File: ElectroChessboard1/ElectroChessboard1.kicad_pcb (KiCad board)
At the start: 2 copper layers, 306.2 x 314.8 mm, 243 parts, among them IC1 A3213ELHLT-T, IC10 A3213ELHLT-T, IC11 A3213ELHLT-T, IC12 A3213ELHLT-T, IC13 A3213ELHLT-T, IC14 A3213ELHLT-T, IC15 A3213ELHLT-T, IC16 A3213ELHLT-T, IC17 A3213ELHLT-T, IC18 ADG708BRUZ-REEL7, IC19 A3213ELHLT-T, IC2 A3213ELHLT-T, IC20 A3213ELHLT-T, IC21 A3213ELHLT-T, IC22 A3213ELHLT-T, IC23 A3213ELHLT-T, IC24 A3213ELHLT-T, IC25 A3213ELHLT-T, IC26 A3213ELHLT-T, IC27 A3213ELHLT-T, IC28 A3213ELHLT-T, IC29 A3213ELHLT-T, IC3 A3213ELHLT-T, IC30 A3213ELHLT-T, IC31 A3213ELHLT-T, IC32 A3213ELHLT-T, IC33 A3213ELHLT-T, IC34 A3213ELHLT-T, IC35 ADG708BRUZ-REEL7, IC36 ADG708BRUZ-REEL7, IC37 A3213ELHLT-T, IC38 A3213ELHLT-T, IC39 A3213ELHLT-T, IC4 A3213ELHLT-T, IC40 A3213ELHLT-T, IC41 A3213ELHLT-T, IC42 A3213ELHLT-T, IC43 A3213ELHLT-T, IC44 A3213ELHLT-T, IC45 A3213ELHLT-T, IC46 A3213ELHLT-T, IC47 A3213ELHLT-T, IC48 A3213ELHLT-T, IC49 A3213ELHLT-T, IC5 A3213ELHLT-T, IC50 A3213ELHLT-T, IC51 A3213ELHLT-T, IC52 A3213ELHLT-T, IC53 ADG708BRUZ-REEL7, IC54 ADG708BRUZ-REEL7, IC55 A3213ELHLT-T, IC56 A3213ELHLT-T, IC57 A3213ELHLT-T, IC58 A3213ELHLT-T, IC59 A3213ELHLT-T, IC6 A3213ELHLT-T, IC60 A3213ELHLT-T, IC61 A3213ELHLT-T, IC62 A3213ELHLT-T, IC63 A3213ELHLT-T, IC64 A3213ELHLT-T, IC65 A3213ELHLT-T, IC66 A3213ELHLT-T, IC67 A3213ELHLT-T, IC68 A3213ELHLT-T, IC69 A3213ELHLT-T, IC7 A3213ELHLT-T, IC70 A3213ELHLT-T, IC71 ADG708BRUZ-REEL7, IC72 ADG708BRUZ-REEL7, IC73 CD74HC154M96, IC74 CD74HC154M96, IC75 DS1307Z+T&R, IC76 CD74HC154M96, IC77 CD74HC154M96, IC8 A3213ELHLT-T, IC9 ADG708BRUZ-REEL7, J2 TYPE-C-31-M-12, J3 Conn_01x04_Pin, J5 Conn_01x06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

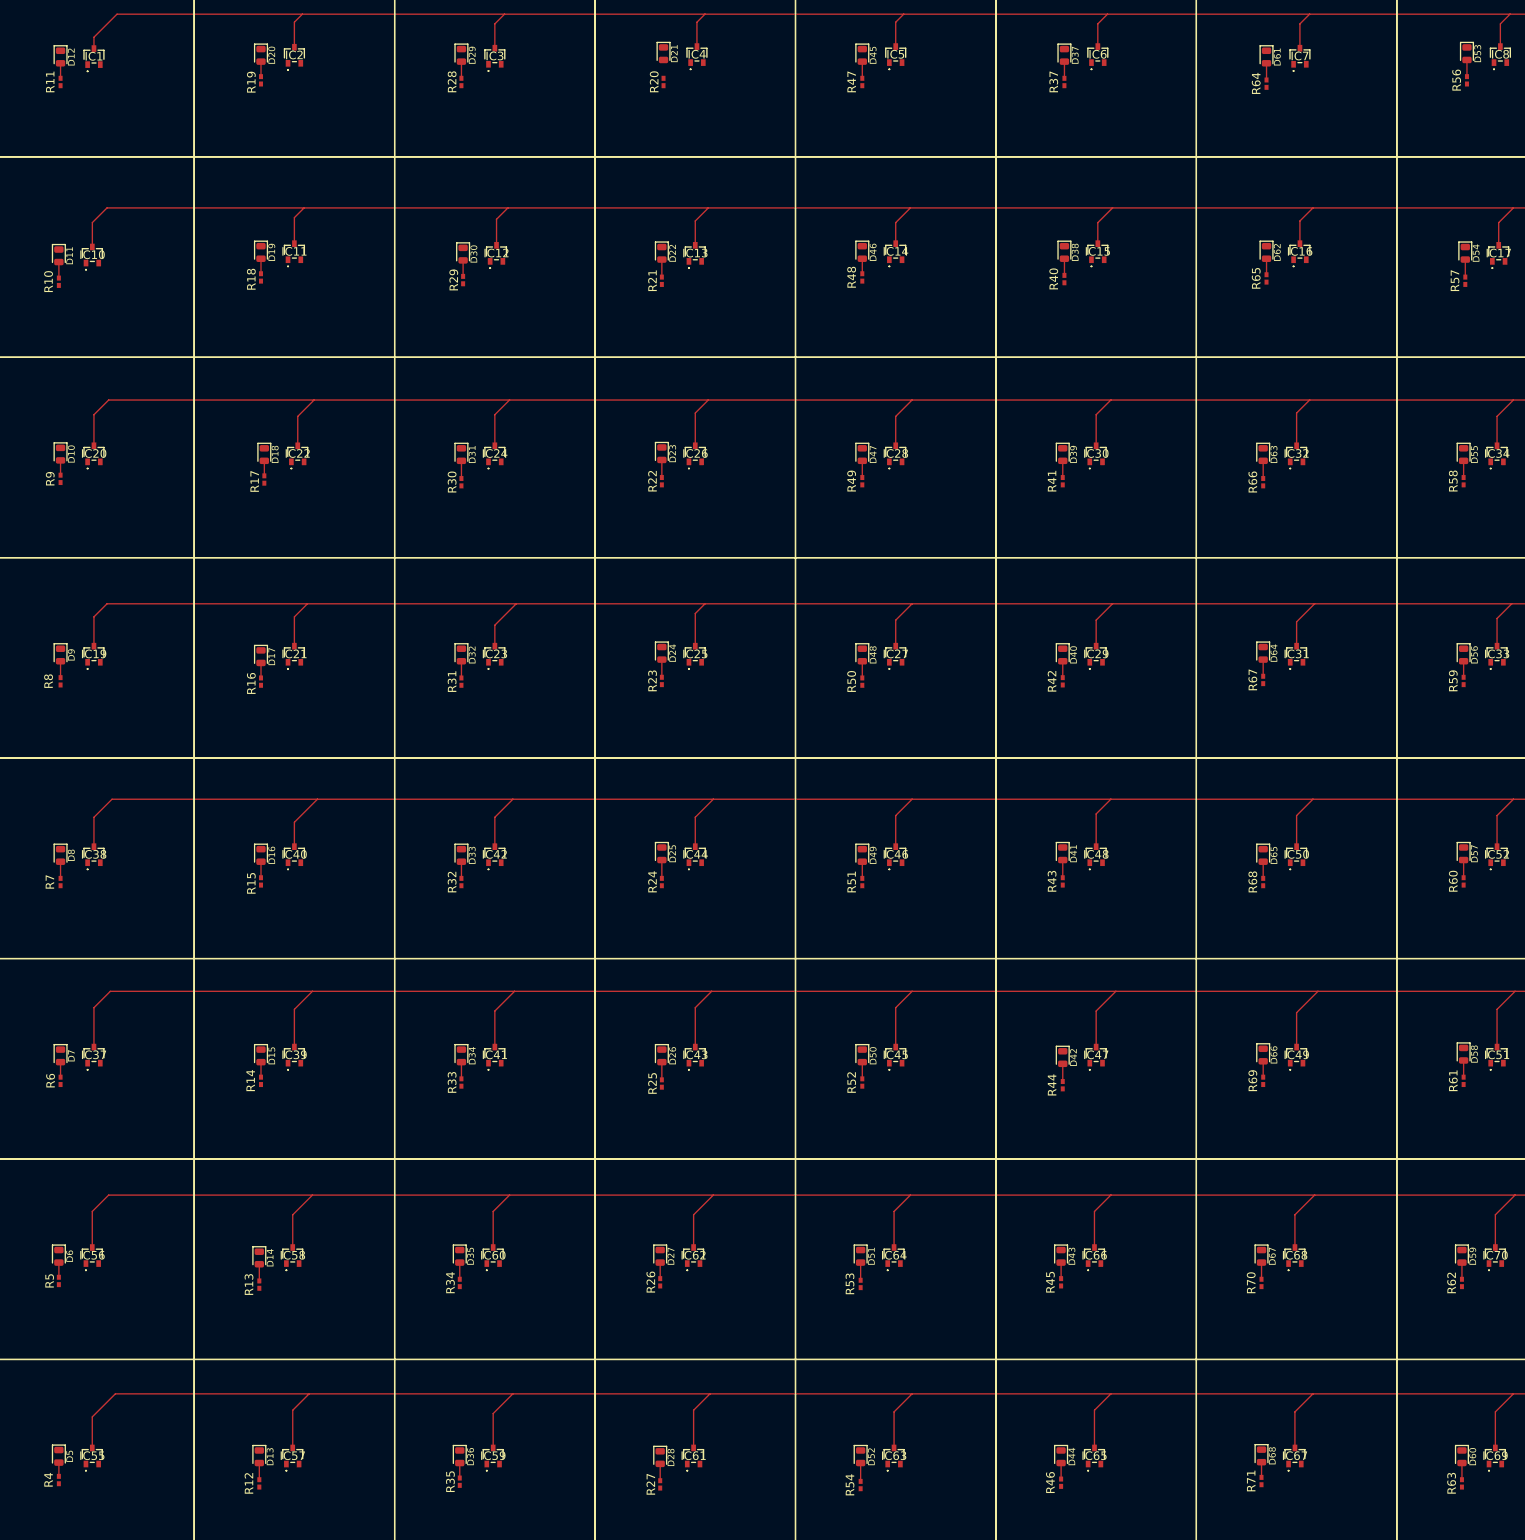
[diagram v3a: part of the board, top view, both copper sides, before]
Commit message: Rotated all LEDs on PCB 180 degrees
.
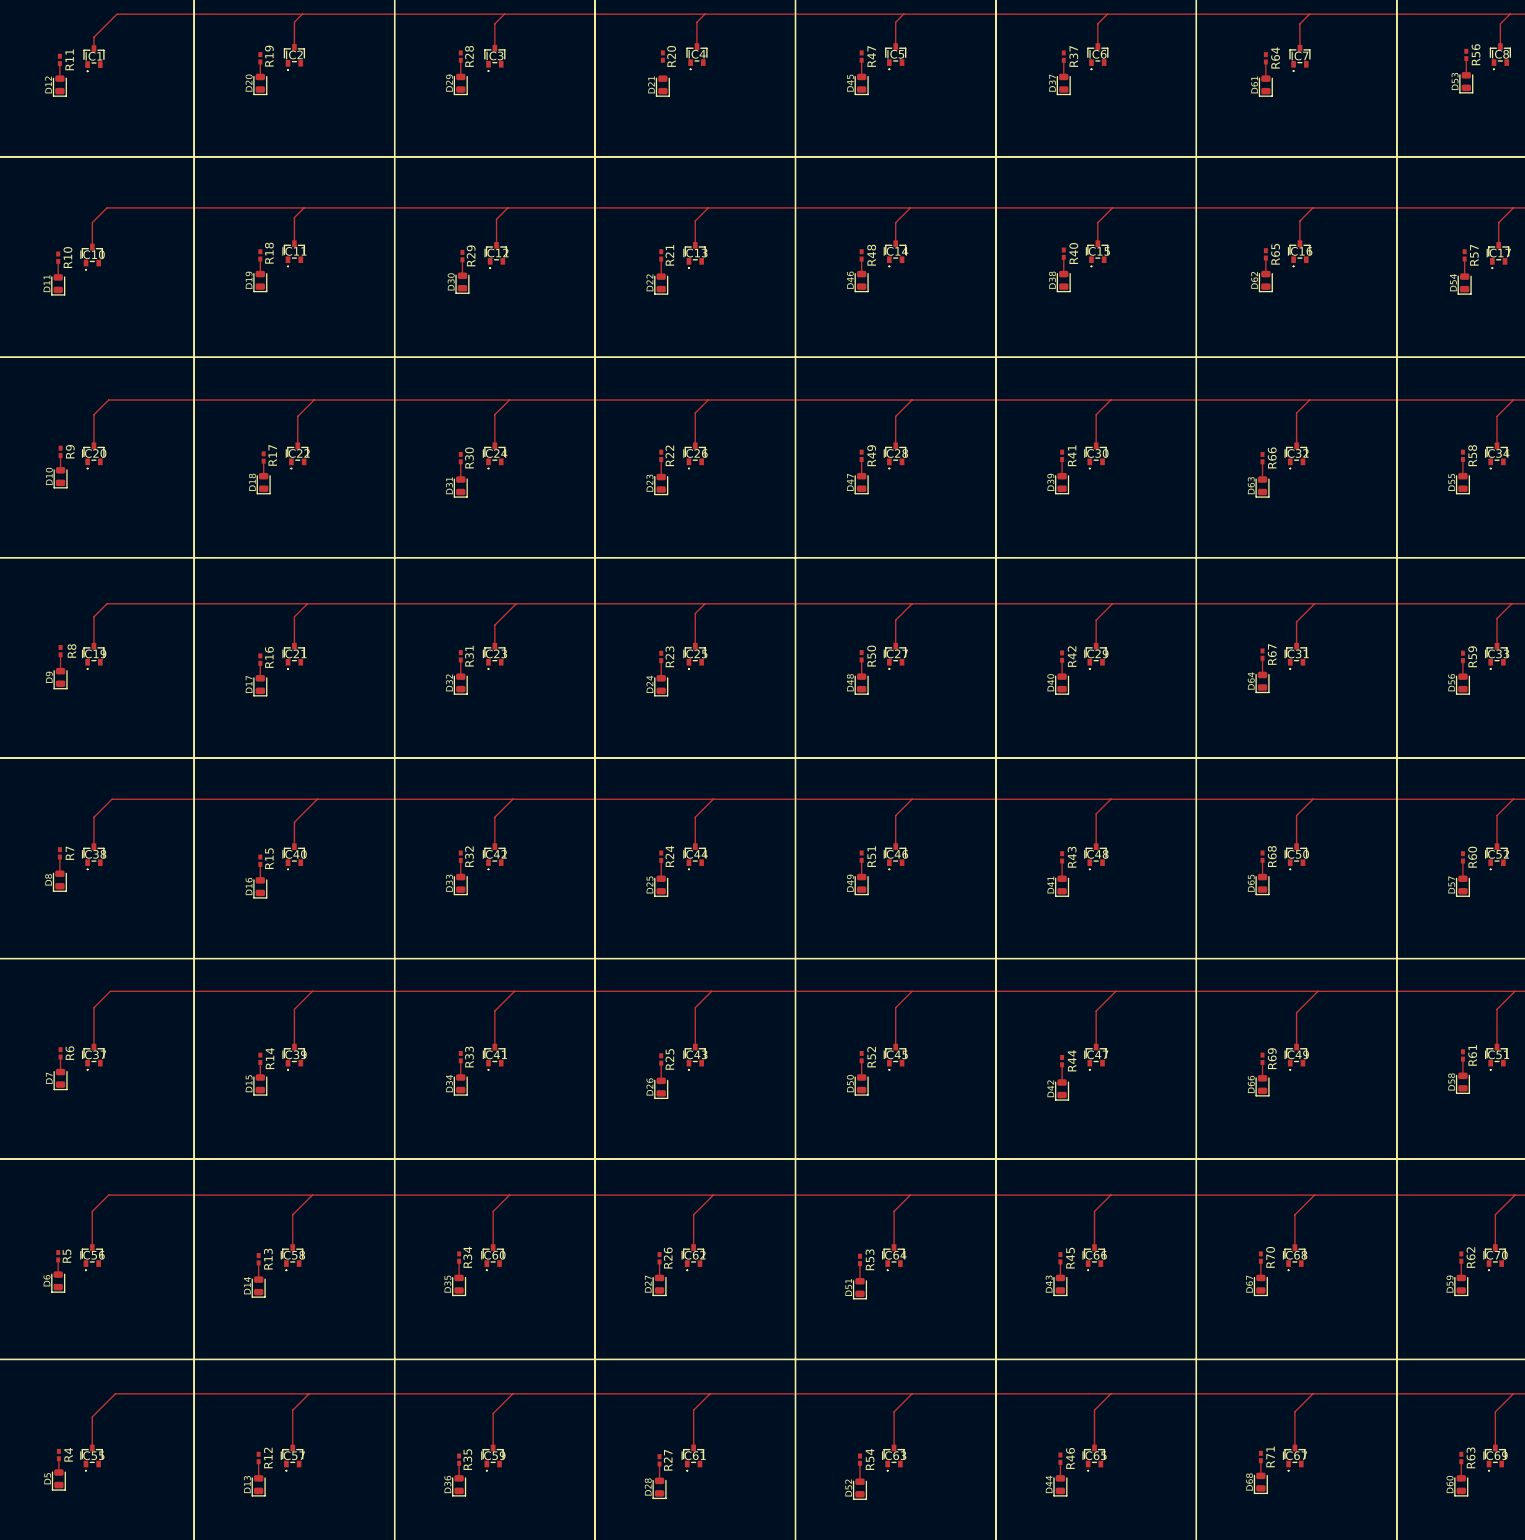
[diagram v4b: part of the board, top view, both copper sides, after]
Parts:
- moved D16 4.68 mm to (69.5, 169.8), turned to 90 degrees
- moved D24 4.68 mm to (129.4, 139.6), turned to 90 degrees
- moved D25 4.68 mm to (129.4, 169.6), turned to 90 degrees
- moved D26 4.68 mm to (129.4, 199.8), turned to 90 degrees
- moved D31 4.68 mm to (99.5, 109.8), turned to 90 degrees
- moved D41 4.68 mm to (189.4, 169.6), turned to 90 degrees
- moved D42 4.68 mm to (189.4, 200.1), turned to 90 degrees
- moved D51 4.68 mm to (159.2, 229.8), turned to 90 degrees
- moved D57 4.68 mm to (249.4, 169.6), turned to 90 degrees
- moved D63 4.68 mm to (219.4, 109.8), turned to 90 degrees
- moved D21 4.68 mm to (129.7, 49.8), turned to 90 degrees
- moved D52 4.68 mm to (159.2, 259.8), turned to 90 degrees
- moved R8 4.51 mm to (39.5, 134.6), turned to 90 degrees
- moved D22 4.43 mm to (129.4, 79.5), turned to 90 degrees
- moved D23 4.43 mm to (129.4, 109.5), turned to 90 degrees
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
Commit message: leds positioned
.
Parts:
- moved D42 5.03 mm to (189.4, 195.1)
- moved R44 5.02 mm to (189.4, 190.9)
- moved D63 4.84 mm to (219.4, 105.0)
- moved R66 4.84 mm to (219.4, 100.9)
- moved D31 4.78 mm to (99.5, 105.1)
- moved R30 4.78 mm to (99.5, 100.9)
- moved D16 4.53 mm to (69.5, 165.3)
- moved D25 4.53 mm to (129.5, 165.1)
- moved D33 4.53 mm to (99.5, 164.8)
- moved D41 4.53 mm to (189.5, 165.1)
- moved D49 4.53 mm to (159.5, 164.8)
- moved D57 4.53 mm to (249.5, 165.1)
- moved D65 4.53 mm to (219.5, 164.8)
- moved R24 4.53 mm to (129.5, 160.8)
- moved R32 4.53 mm to (99.5, 160.8)
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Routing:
- net SafeGND: track 2392.7 -> 2423.4 mm
- net Net-(D10-A): track 2.21 -> 2.88 mm

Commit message: Wired demuxes to leds
.
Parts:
- moved U2 239.5 mm to (451.5, 360.0)
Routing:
- net Net-(D12-K): track 0.00 -> 313.4 mm
- net Net-(D20-K): track 0.00 -> 295.3 mm, vias 0 -> 2
- net Net-(D29-K): track 0.00 -> 289.8 mm, vias 0 -> 4
- net Net-(D11-K): track 0.00 -> 281.7 mm
- net Net-(D19-K): track 0.00 -> 268.2 mm, vias 0 -> 2
- net Net-(D61-K): track 0.00 -> 264.8 mm, vias 0 -> 14
- net Net-(D30-K): track 0.00 -> 258.4 mm, vias 0 -> 4
- net Net-(D53-K): track 0.00 -> 257.0 mm, vias 0 -> 2
- net Net-(D37-K): track 0.00 -> 256.8 mm, vias 0 -> 2
- net Net-(D45-K): track 0.00 -> 256.2 mm, vias 0 -> 8
- net Net-(D21-K): track 0.00 -> 254.0 mm, vias 0 -> 2
- net Net-(D10-K): track 0.00 -> 249.8 mm
- net Net-(D18-K): track 0.00 -> 240.0 mm, vias 0 -> 2
- net Net-(D62-K): track 0.00 -> 232.9 mm, vias 0 -> 12
- net Net-(D38-K): track 0.00 -> 228.6 mm, vias 0 -> 2
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
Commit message: Muxes and demuxes wired to halls and leds
.
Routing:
- net Net-(IC37-VOUT): track 0.00 -> 252.3 mm, vias 0 -> 4
- net Net-(IC56-VOUT): track 0.00 -> 252.3 mm, vias 0 -> 8
- net Net-(IC55-VOUT): track 0.00 -> 252.1 mm, vias 0 -> 14
- net Net-(IC38-VOUT): track 0.00 -> 251.8 mm, vias 0 -> 8
- net Net-(IC19-VOUT): track 0.00 -> 250.4 mm, vias 0 -> 6
- net Net-(IC20-VOUT): track 0.00 -> 249.5 mm, vias 0 -> 6
- net Net-(IC1-VOUT): track 0.00 -> 248.9 mm, vias 0 -> 8
- net Net-(IC10-VOUT): track 0.00 -> 248.6 mm, vias 0 -> 8
- net Net-(IC58-VOUT): track 0.00 -> 224.0 mm, vias 0 -> 6
- net Net-(IC39-VOUT): track 0.00 -> 224.0 mm, vias 0 -> 2
- net Net-(IC57-VOUT): track 0.00 -> 223.9 mm, vias 0 -> 12
- net Net-(IC40-VOUT): track 0.00 -> 223.3 mm, vias 0 -> 6
- net Net-(IC21-VOUT): track 0.00 -> 222.7 mm, vias 0 -> 4
- net Net-(IC11-VOUT): track 0.00 -> 220.6 mm, vias 0 -> 6
- net Net-(IC2-VOUT): track 0.00 -> 220.6 mm, vias 0 -> 6
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
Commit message: Wired power, partially CPU too
.
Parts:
- moved C10 196.8 mm to (292.0, 254.0), turned to -90 degrees
- moved C1 194.1 mm to (284.5, 330.2)
- moved C3 193.0 mm to (284.5, 328.3)
- moved U3 189.7 mm to (300.0, 253.5)
- moved FB1 181.7 mm to (310.0, 258.5), turned to -90 degrees
- moved C4 179.5 mm to (292.5, 289.2), turned to 180 degrees
- moved F1 177.8 mm to (310.0, 272.4), turned to -90 degrees
- moved C5 175.1 mm to (312.8, 255.8), turned to 180 degrees
- moved Y1 171.4 mm to (294.5, 325.5)
- moved D2 168.7 mm to (310.0, 265.0), turned to 90 degrees
- moved C8 167.5 mm to (313.5, 285.0), turned to 180 degrees
- moved C9 152.3 mm to (315.2, 278.5)
- moved D4 96.2 mm to (312.8, 253.0)
- moved R73 94.7 mm to (313.1, 242.0), turned to 180 degrees
- moved R72 94.5 mm to (313.1, 239.3)
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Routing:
- net SafeGND: track 2470.4 -> 3060.2 mm, vias 2 -> 8
- net SafeVCC: track 0.00 -> 324.4 mm, vias 0 -> 7
- net FT232RLtx: track 0.00 -> 94.9 mm, vias 0 -> 2
- net FT232RLrx: track 0.00 -> 87.0 mm, vias 0 -> 2
- net FT232RLreset: track 0.00 -> 75.6 mm
- net Net-(U1-XTAL1): track 0.00 -> 50.2 mm
- net Net-(U1-XTAL2): track 0.00 -> 27.3 mm
- net Net-(J2-DP1): track 0.00 -> 26.9 mm, vias 0 -> 2
- net VBUS: track 0.00 -> 26.0 mm
- net Net-(J2-DN1): track 0.00 -> 24.3 mm, vias 0 -> 2
- net Net-(J2-CC1): track 0.00 -> 15.2 mm
- net Net-(J2-CC2): track 0.00 -> 10.1 mm
- net Net-(U1-AREF): track 0.00 -> 7.08 mm
- net Net-(U3-DTR): track 0.00 -> 6.99 mm
- net Net-(D2-K): track 0.00 -> 4.50 mm
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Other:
- board text added: "GND"
- board text added: "VCC"
